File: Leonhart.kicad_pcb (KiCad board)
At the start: 8 copper layers, 404 parts, among them J1001 TC2050, J1002 Conn_01x03_Pin, J2001 TC2050, J2002 Conn_01x06_Pin, J2003 SMA-KWE901, J3002 TC2050, J3003 Conn_01x06_Pin, J3004 SMA-KWE901, J7001 USB_C_Receptacle_USB2.0_16P, J7002 USB_A, J7003 Micro_SD_Card_Det1, Q3001 DMG1012T, Q6001 DMG1012T, Q6002 DMG1012T, U1001 AM6231ASGGGAALW, U1002 SN74LVC2G241DCUR, U1003 AT24C32D-STUM-T, U2001 CC2652PSIP, U3001 nRF52840, U4001 TPS6521903RHBR, U4002 TLV62595DMQR, U5001 K4AAG165WA-BCWE, U6001 HR911130A, U6002 RTL8211F-CG, U7001 TVS0500DRVR, U7002 EMMC16G-TB29-PZ90, U7004 TPD3S014, U7005 TPS22918DBVR, X1001 32.768kHz, X1002 25MHz, X3001 32.768kHz, X3002 25MHz, X6001 ECS-2520MV-250-BN-TR

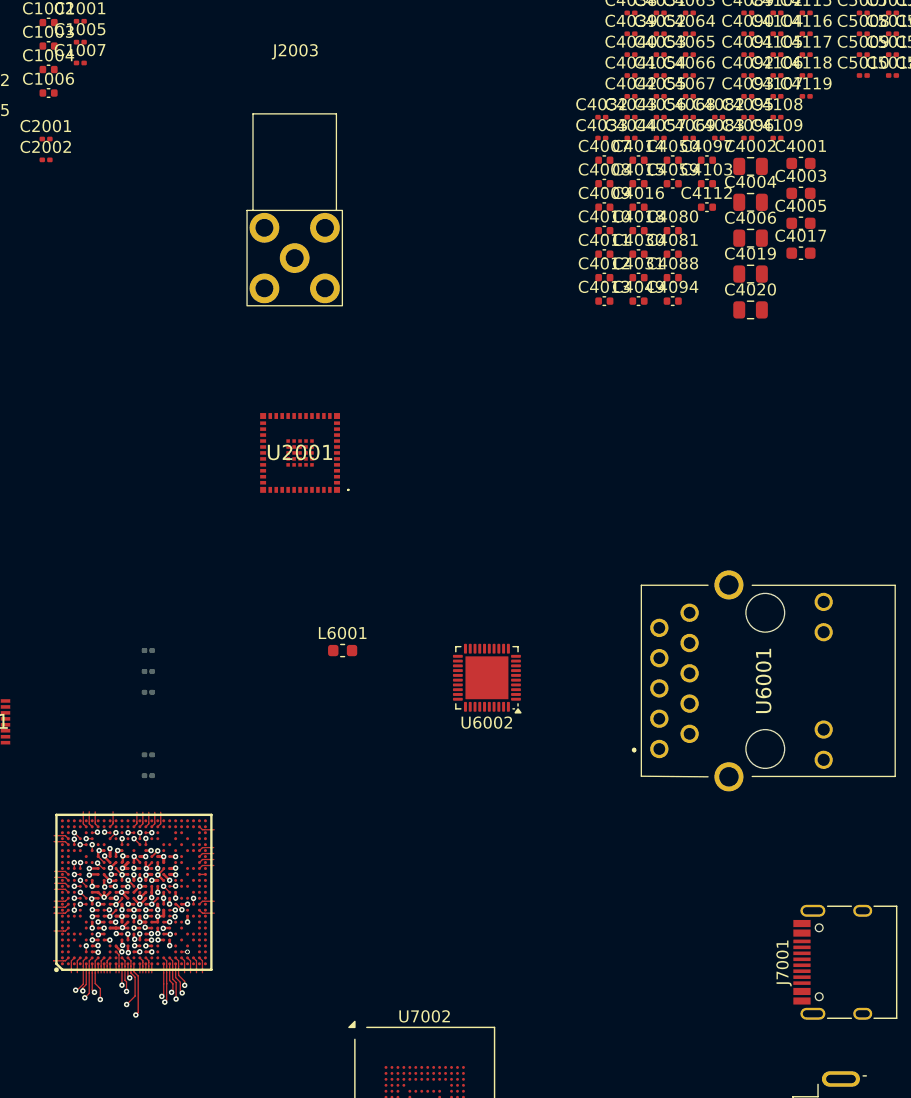
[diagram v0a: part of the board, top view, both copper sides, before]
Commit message: Did more SoC power decoupling routing
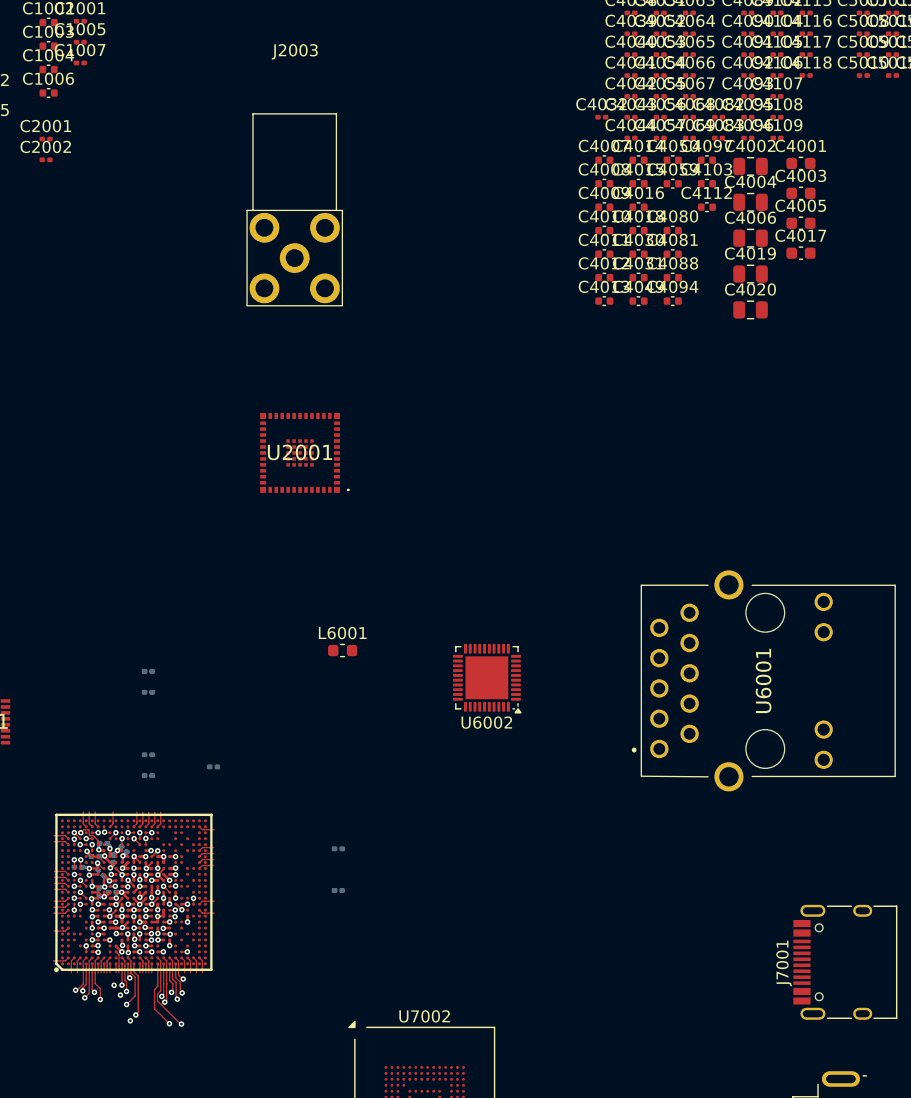
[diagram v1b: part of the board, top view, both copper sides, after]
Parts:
- added C4021: 1u, Capacitor_SMD:C_0201_0603Metric, B.Cu at (145.9, 131.1)
- added C4022: 1u, Capacitor_SMD:C_0201_0603Metric, B.Cu at (147.1, 128.3)
- added C4026: 1u, Capacitor_SMD:C_0201_0603Metric, B.Cu at (146.0, 129.5)
- added C4027: 1u, Capacitor_SMD:C_0201_0603Metric, B.Cu at (146.2, 127.0)
- added C4061: 0.1u, Capacitor_SMD:C_0201_0603Metric, B.Cu at (145.5, 128.1)
- added C4062: 0.1u, Capacitor_SMD:C_0201_0603Metric, B.Cu at (166.0, 127.5)
- added C4073: 0.1u, Capacitor_SMD:C_0201_0603Metric, B.Cu at (148.0, 127.5)
- added C4074: 0.1u, Capacitor_SMD:C_0201_0603Metric, B.Cu at (166.0, 131.0)
- C4033, C4119: moved to B.Cu
- moved C4119 89.0 mm to (144.1, 129.0), turned to 180 degrees
- moved C4033 75.4 mm to (147.0, 131.1), turned to 180 degrees
- moved C4023 11.2 mm to (155.5, 120.6), turned to 0 degrees
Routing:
- net /Memory [5]/DDR_DQ13: track 1.13 -> 49.7 mm
- net /Memory [5]/DDR_DQ9: track 0.57 -> 45.7 mm, vias 1 -> 2
- net /Memory [5]/DDR_DQ11: track 1.05 -> 46.0 mm
- net /Memory [5]/DDR_DQ15: track 3.12 -> 42.4 mm
- net /Memory [5]/DDR_DQ8: track 0.57 -> 31.4 mm, vias 1 -> 2
- net /Memory [5]/DDR_DQ10: track 0.57 -> 31.2 mm, vias 1 -> 2
- net /Memory [5]/DDR_DQ14: track 3.24 -> 33.2 mm
- net /Memory [5]/DDR_DQ12: track 4.25 -> 30.2 mm
- net GND: track 38.4 -> 41.3 mm, vias 40 -> 44
- net CC2652_RSTn: track 0.00 -> 2.51 mm, vias 0 -> 1
- net VDDSHV5_SDIO: track 0.74 -> 1.40 mm
- net /Power Circuitry [4]/CAP_VDDS5: track 0.74 -> 1.36 mm
- net /Memory [5]/DDR_LDM: track 41.8 -> 42.4 mm
- net /Memory [5]/DDR_UDM: track 35.2 -> 34.6 mm
- net /Power Circuitry [4]/CAP_VDDS1: track 0.66 -> 1.20 mm
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
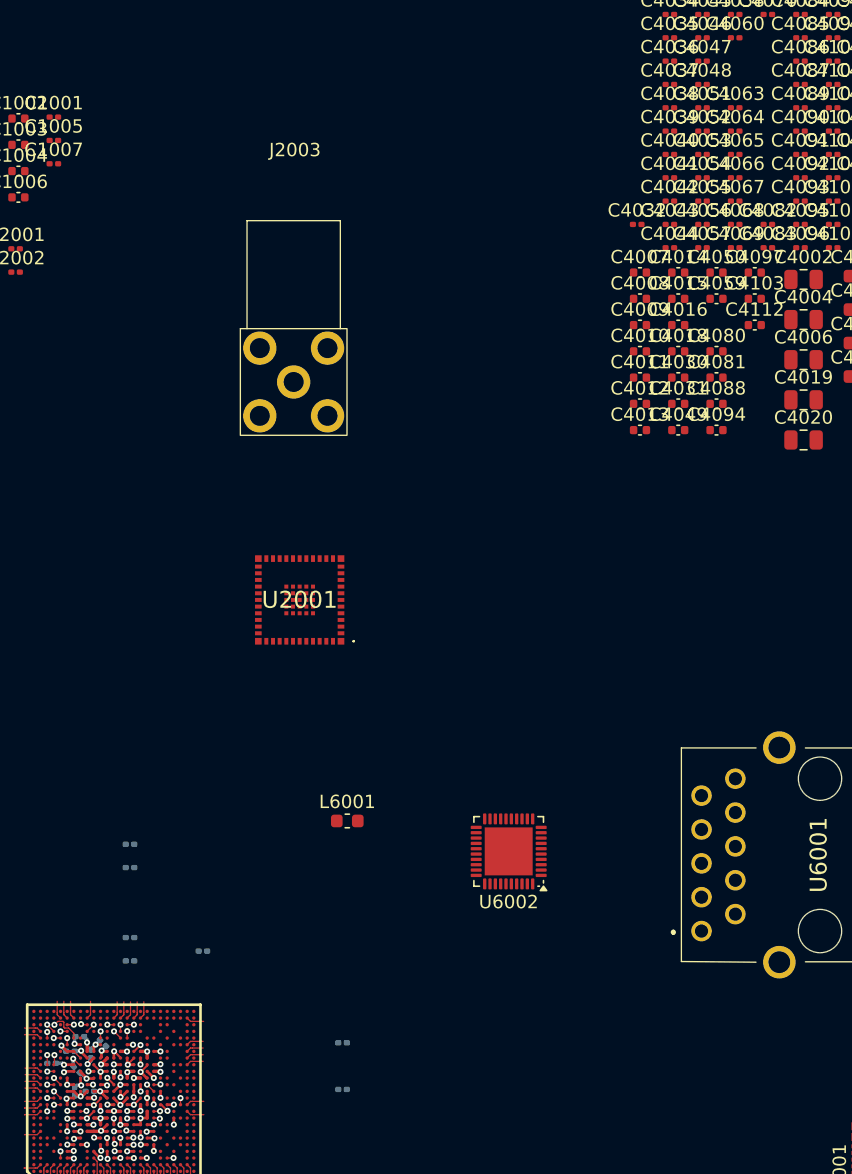
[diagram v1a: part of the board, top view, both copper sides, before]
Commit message: More SoC power cap placement
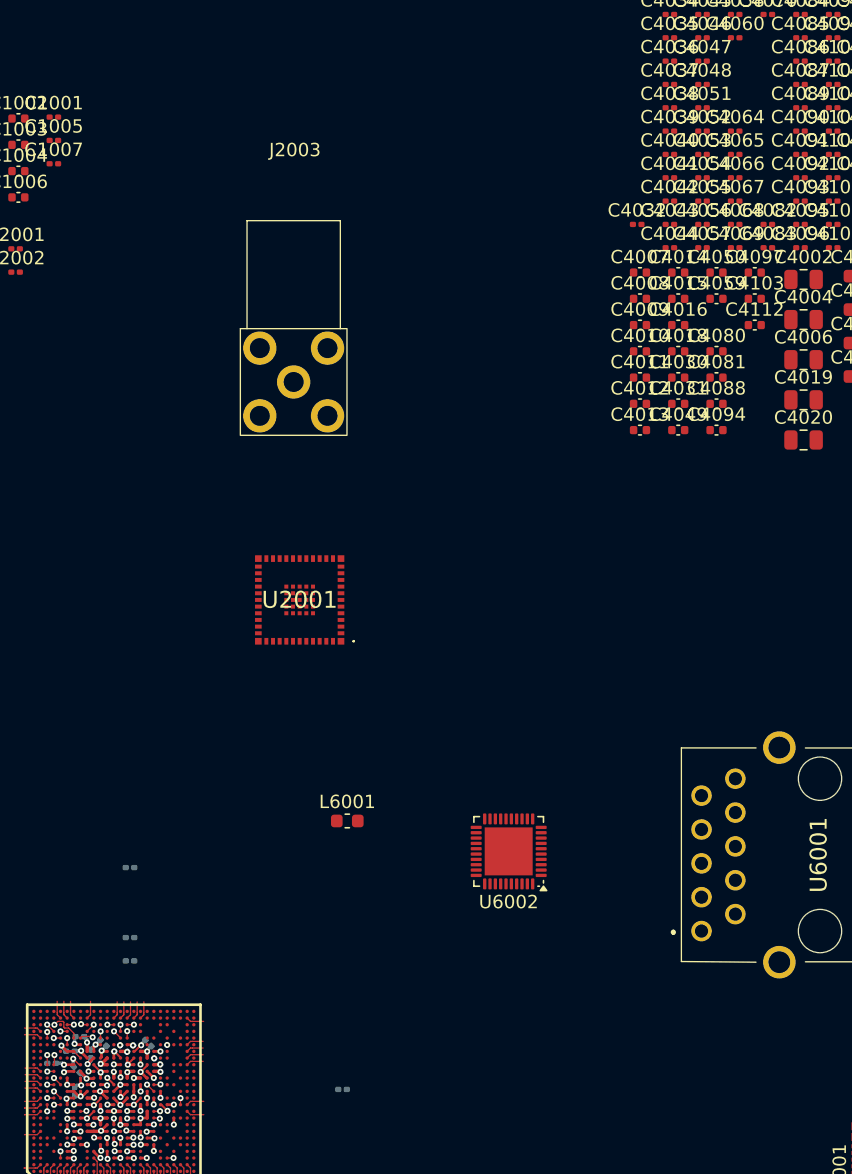
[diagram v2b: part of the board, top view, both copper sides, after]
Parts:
- C4063: moved to B.Cu
- moved C4063 82.8 mm to (151.4, 127.5), turned to -45 degrees
- moved C4062 16.9 mm to (149.1, 127.9), turned to 45 degrees
- moved C4024 15.3 mm to (150.0, 127.9), turned to 45 degrees
- moved C4023 8.96 mm to (152.1, 128.9), turned to 135 degrees
- moved C4033 1.92 mm to (147.8, 129.4), turned to 90 degrees
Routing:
- net UART5_RXD: track 0.00 -> 1.00 mm, vias 0 -> 1
- net GND: track 41.3 -> 42.0 mm, vias 44 -> 47
- net VDD_1V8: track 6.79 -> 7.36 mm

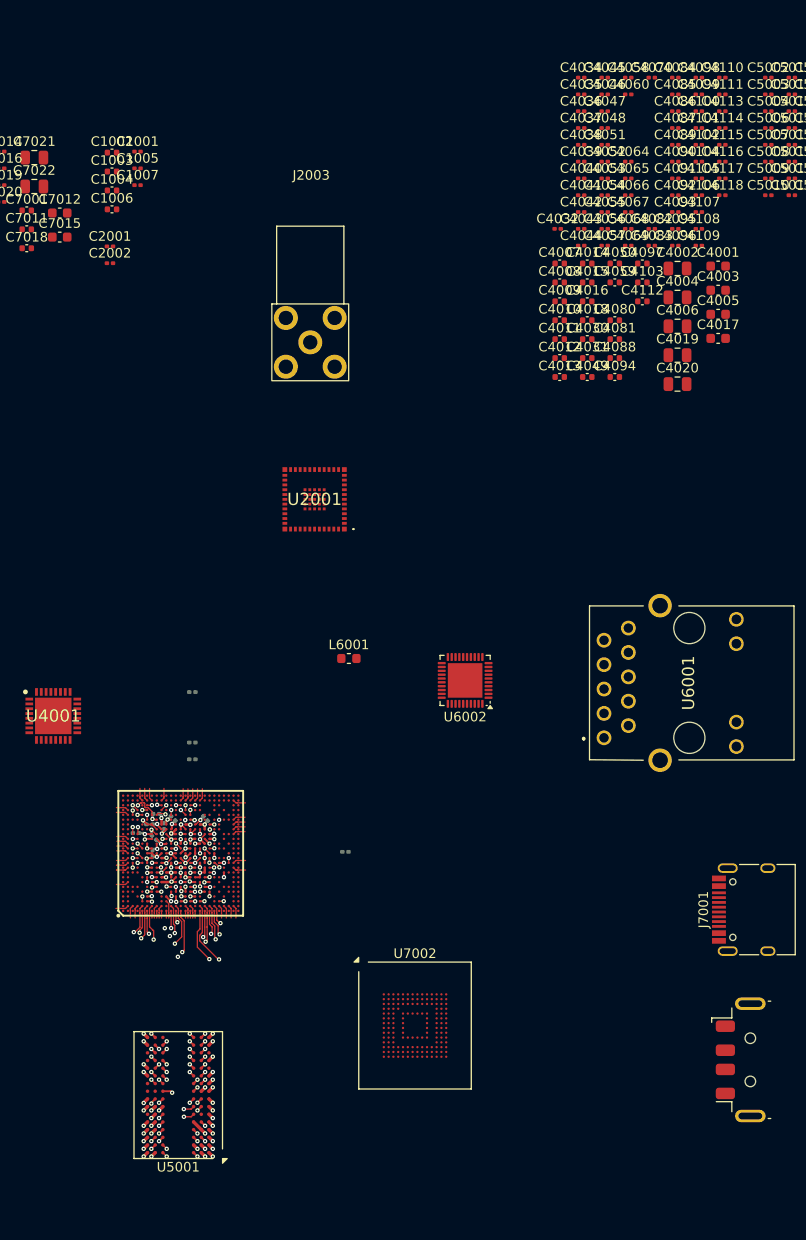
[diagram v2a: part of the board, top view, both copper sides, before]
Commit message: Cleaned up schematic
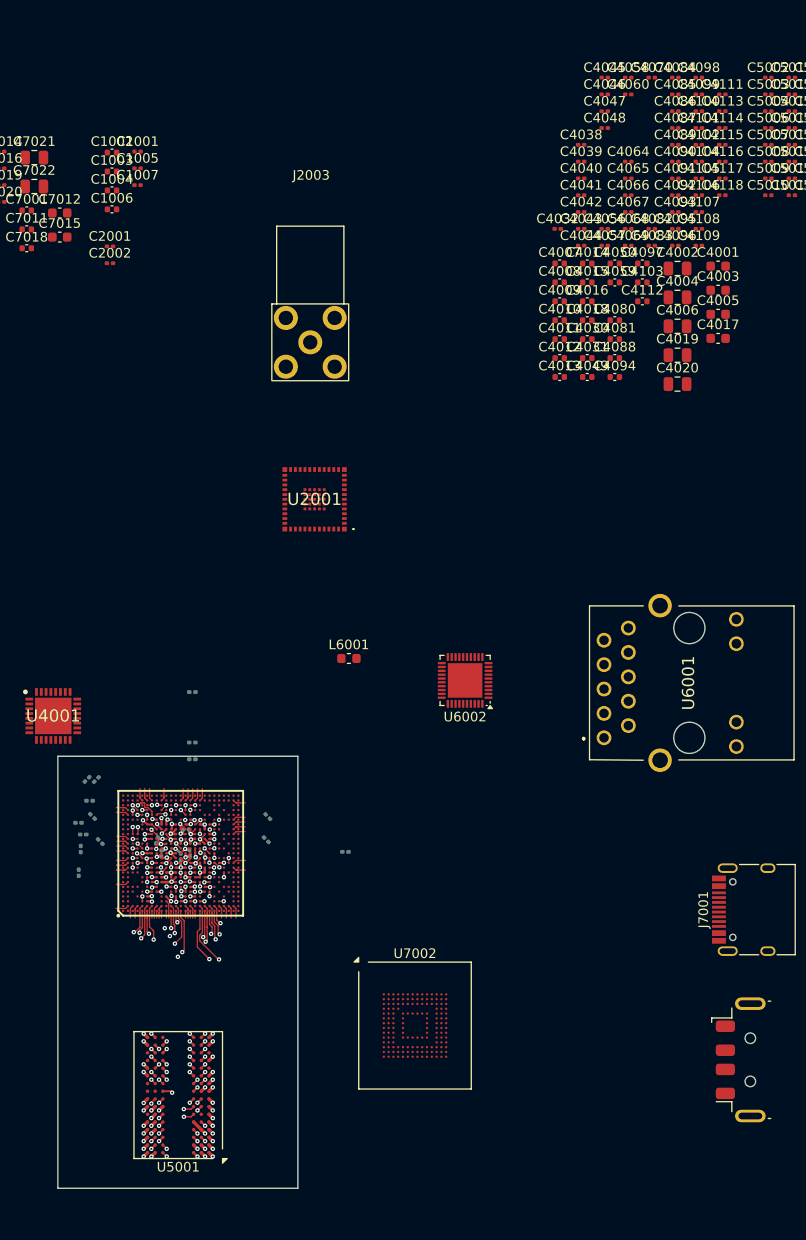
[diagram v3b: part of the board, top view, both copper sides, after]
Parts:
- C4034, C4035, C4036, C4037, C4051, C4052, C4053, C4054, C4055, C4110: moved to B.Cu
- moved C4110 98.8 mm to (148.8, 131.4), turned to -90 degrees
- moved C4035 88.9 mm to (149.7, 131.1), turned to -86 degrees
- moved C4034 88.5 mm to (149.4, 128.6)
- moved C4036 87.7 mm to (150.4, 131.8), turned to 90 degrees
- moved C4037 87.3 mm to (146.8, 131.1), turned to -90 degrees
- moved C4051 85.1 mm to (148.6, 129.9), turned to 35 degrees
- moved C4053 83.2 mm to (146.3, 129.8), turned to -105 degrees
- moved C4052 83.0 mm to (149.6, 129.9), turned to 35 degrees
- moved C4054 82.4 mm to (147.6, 131.3), turned to 60 degrees
- moved C4055 79.0 mm to (151.1, 131.3), turned to -45 degrees
- moved C4024 11.0 mm to (140.0, 123.4)
- moved C4062 11.0 mm to (139.0, 123.4)
- moved C4022 10.1 mm to (138.2, 133.1)
- moved C4073 7.98 mm to (140.4, 129.9)
- moved C4021 7.49 mm to (138.4, 130.7)
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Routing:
- net VDD_CORE: track 9.81 -> 11.5 mm
- net VDD_1V8: track 7.36 -> 6.49 mm
- net GND: track 42.0 -> 41.2 mm, vias 47 -> 48
- net VDDA_PLL2: track 0.53 -> 1.22 mm
- net VDDSHV5_SDIO: track 1.40 -> 0.74 mm
- net VDDA_0V85: track 4.58 -> 5.23 mm
- net /Power Circuitry [4]/CAP_VDDS5: track 1.36 -> 0.74 mm
- net VDD_3V3: track 4.31 -> 3.76 mm
- net /Power Circuitry [4]/CAP_VDDS1: track 1.20 -> 0.66 mm
- net /Power Circuitry [4]/CAP_VDDS0: track 1.11 -> 0.57 mm
- net /Power Circuitry [4]/CAP_VDDS6: track 1.22 -> 0.68 mm
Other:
- board outline added: 25 x 45 mm

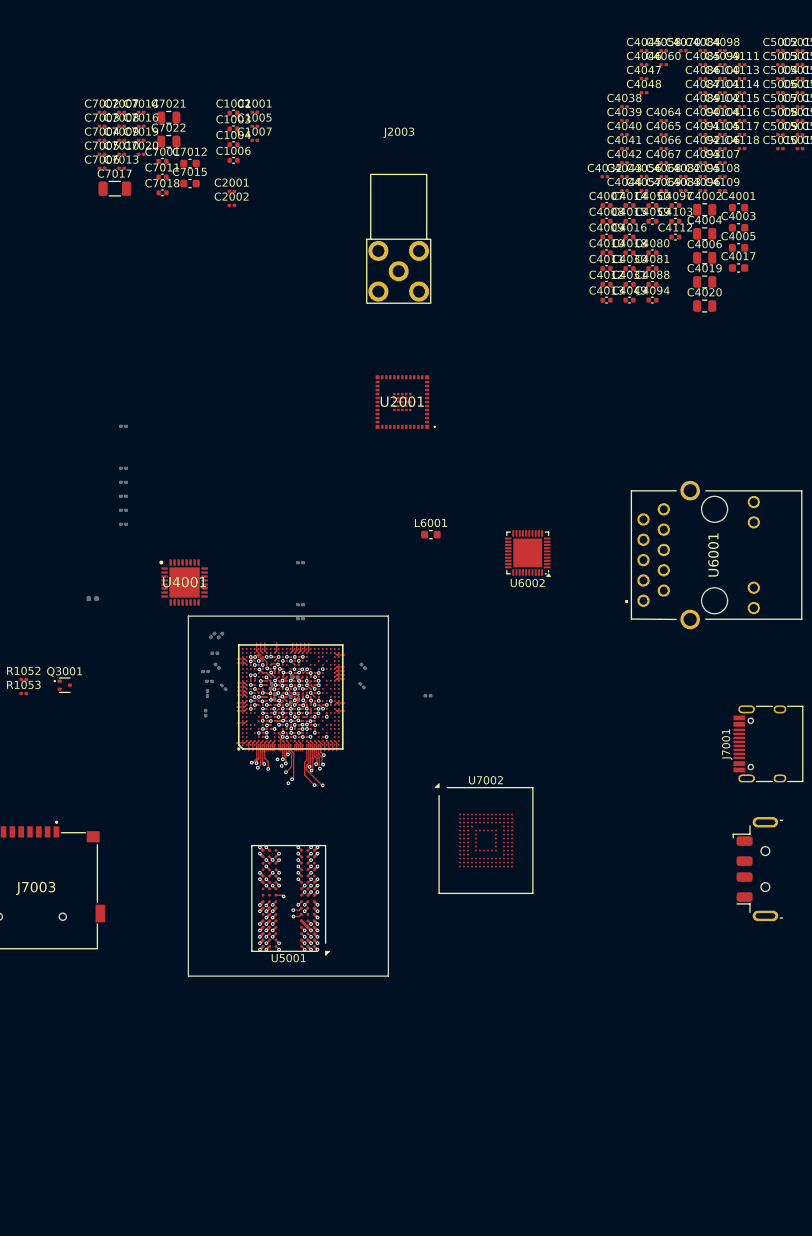
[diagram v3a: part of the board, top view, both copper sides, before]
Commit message: Restarted SoC power decoupling based on manufacturer capabilities
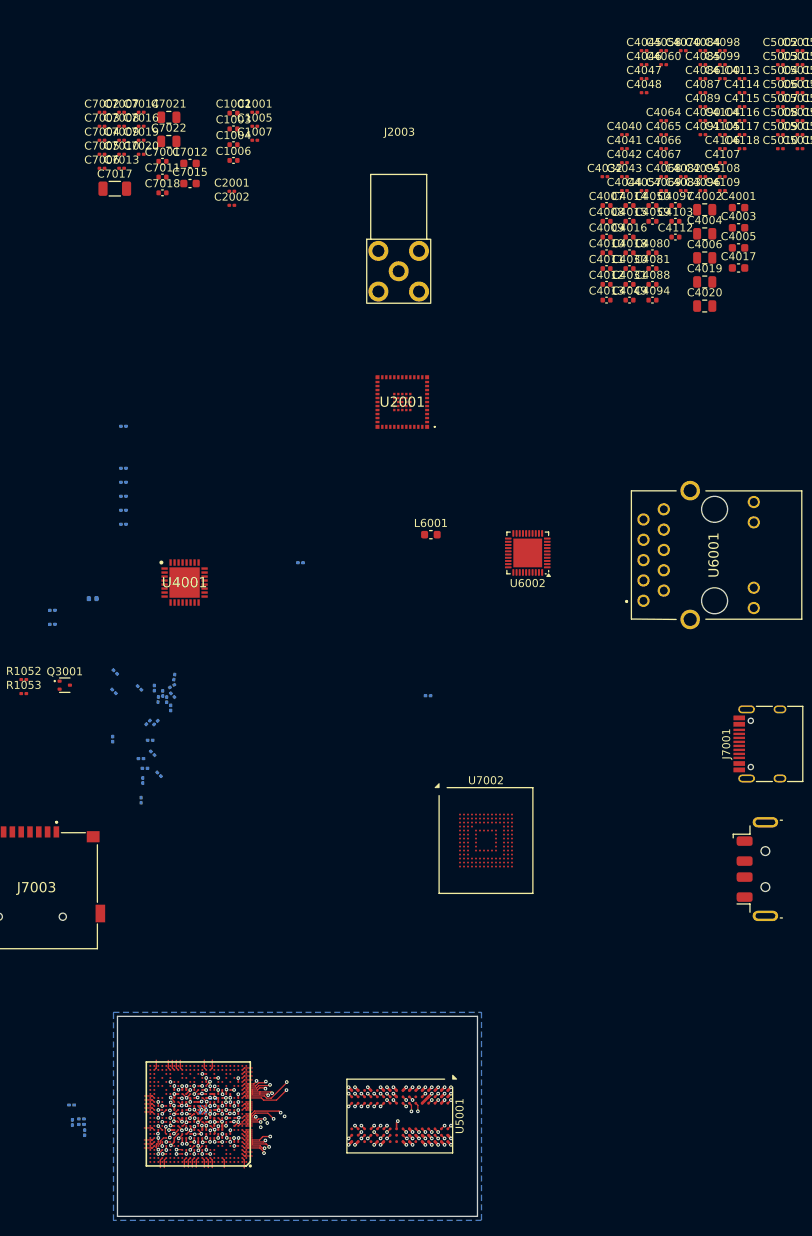
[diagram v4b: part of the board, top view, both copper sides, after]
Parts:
- C4038, C4039, C4056, C4092, C4093, C4101, C4102, C4111: moved to B.Cu
- moved C4111 156.5 mm to (121.5, 184.3), turned to -90 degrees
- moved C4102 149.0 mm to (121.4, 182.1)
- moved C4093 132.0 mm to (139.1, 181.3)
- moved C4101 101.2 mm to (134.0, 129.8), turned to 30 degrees
- moved C4056 96.7 mm to (126.5, 136.4), turned to -90 degrees
- moved C4092 96.5 mm to (133.8, 132.5), turned to -90 degrees
- moved C4039 92.3 mm to (133.3, 131.4), turned to 90 degrees
- moved C4038 90.8 mm to (134.2, 128.6), turned to 80 degrees
- moved C4034 62.0 mm to (122.6, 184.5), turned to 180 degrees
- moved C4033 61.4 mm to (123.0, 185.6), turned to -90 degrees
- moved C4035 59.3 mm to (122.6, 183.8), turned to 180 degrees
- moved C4051 54.3 mm to (137.8, 183.1), turned to 180 degrees
- moved C4052 53.7 mm to (137.8, 182.3), turned to 180 degrees
- moved U1001 53.4 mm to (137.2, 183.2), turned to 180 degrees
- moved C4053 53.4 mm to (138.8, 182.6), turned to -90 degrees
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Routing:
- net GND: track 41.2 -> 38.9 mm, vias 48 -> 50
- net VDD_CORE: track 11.5 -> 9.83 mm
- net VDDA_PLL2: track 1.22 -> 0.53 mm
- added copper zone on B.Cu, net GND
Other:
- board size 25 x 45 mm -> 45 x 25 mm
